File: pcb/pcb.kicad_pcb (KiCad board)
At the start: 2 copper layers, 126 x 50.5 mm, 53 parts, among them J1 Conn_01x02_Socket, J2 Conn_01x04_Socket, U1 AP2112K-3.3TRG1, U2 W25Q16JVUXIQ, U3 RP2040, U4 DS4432U+T&amp;R, U5 AD8403ARUZ1-REEL, U6 ADG801BRTZ-REEL7, Y2 Crystal_GND24_Small

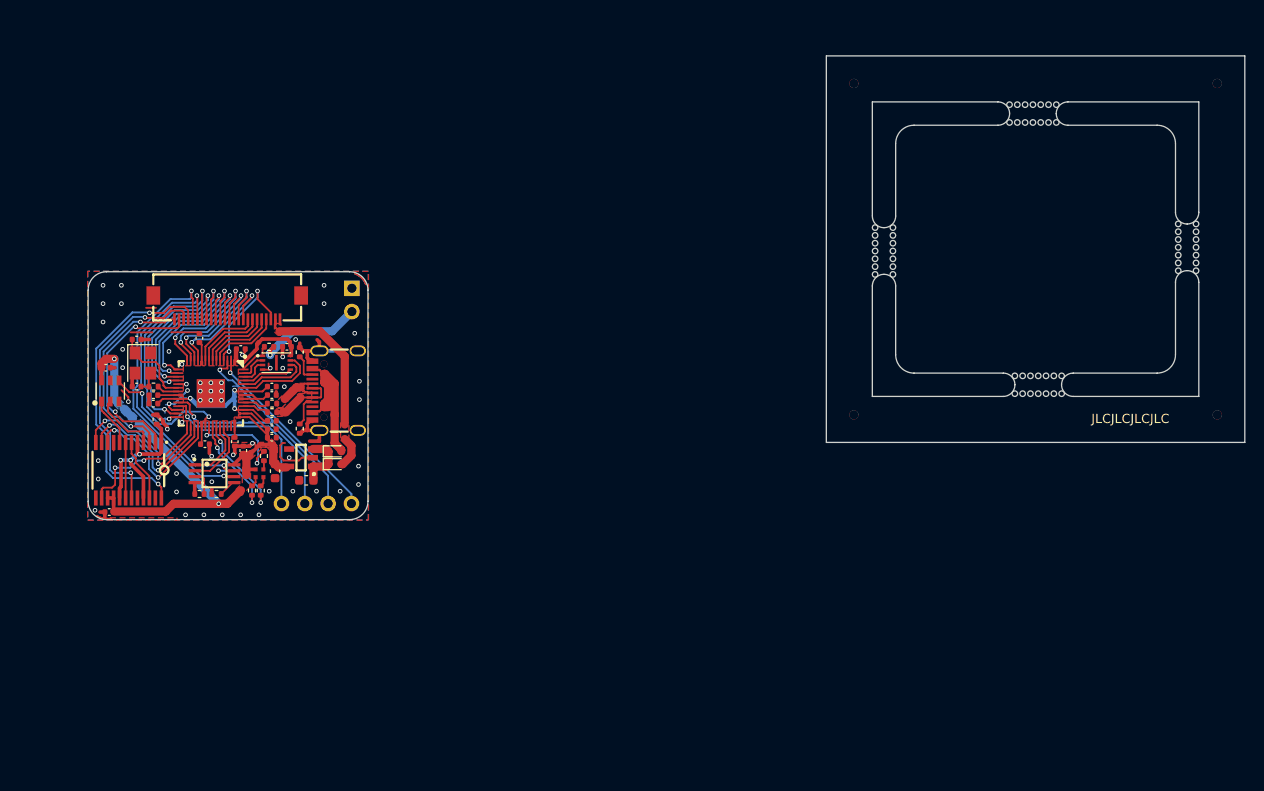
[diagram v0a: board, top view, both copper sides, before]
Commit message: Tweak holes
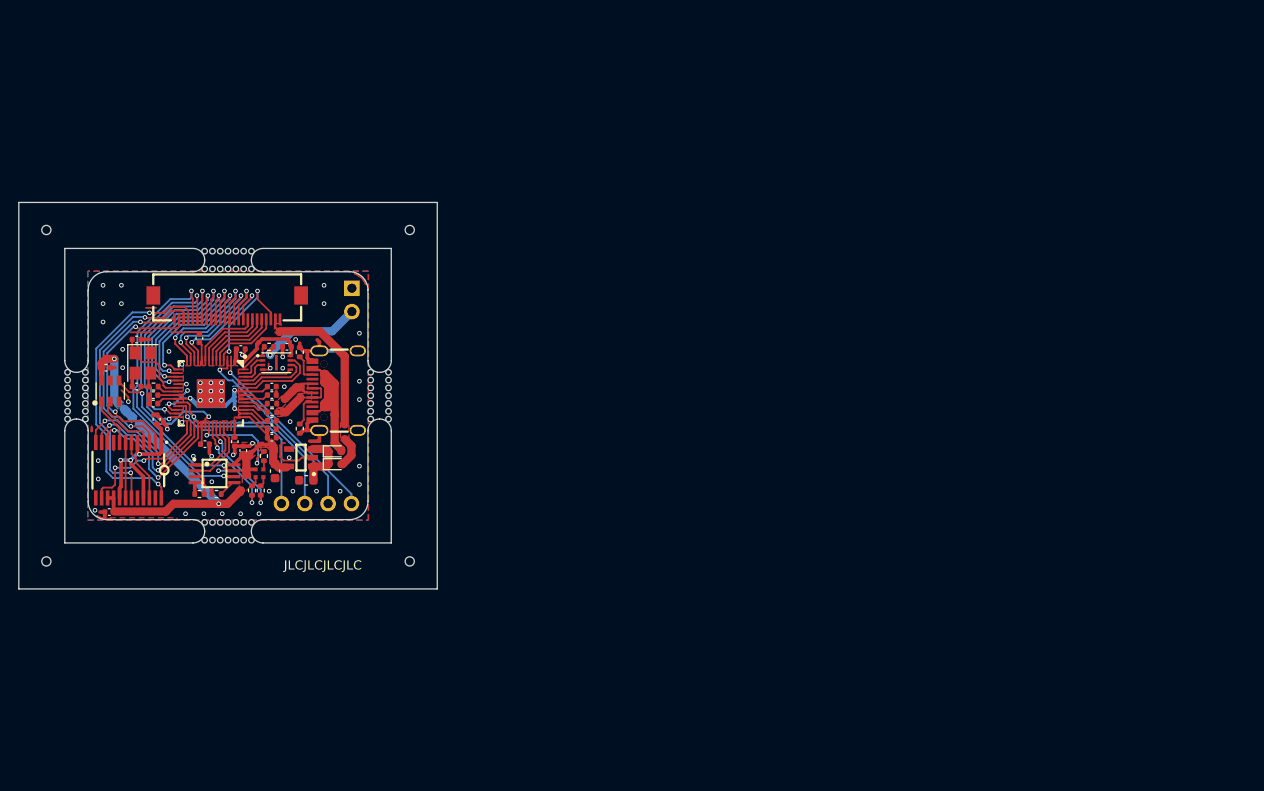
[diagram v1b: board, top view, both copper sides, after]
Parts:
- removed the REF** at (229.6, 29.5)
- removed the REF** at (190.0, 65.6)
- removed the REF** at (190.0, 29.5)
- removed the REF** at (229.6, 65.6)
- added REF**: Hole_1, MouseBites_2.54:Hole_1, F.Cu at (141.6, 81.5)
- added REF**: Hole_1, MouseBites_2.54:Hole_1, F.Cu at (102.0, 81.5)
- added REF**: Hole_1, MouseBites_2.54:Hole_1, F.Cu at (141.6, 45.5)
- added REF**: Hole_1, MouseBites_2.54:Hole_1, F.Cu at (102.0, 45.5)
- moved REF** 89.7 mm to (121.8, 79.5)
- moved REF** 89.4 mm to (139.6, 63.5)
- moved REF** 89.4 mm to (104.1, 63.5)
- moved REF** 89.1 mm to (121.8, 47.5)
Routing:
- net GND: track 53.9 -> 54.9 mm
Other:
- board size 126 x 50.5 mm -> 45.6 x 42.1 mm
- board text added: "Error:5 Warning:5"

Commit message: Resize
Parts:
- moved REF** 20.0 mm to (141.6, 25.4)
- moved REF** 20.0 mm to (102.0, 25.4)
- moved REF** 20.0 mm to (141.6, 101.5)
- moved REF** 20.0 mm to (102.0, 101.5)
- moved C11 1.43 mm to (123.8, 67.8), turned to 0 degrees
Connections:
- net RELAY_A renamed SW_IN
- LED1 pad 1: +3V3 -> LED_ANODE
- R10 pad 1: Net-(U3-GPIO23) -> LED_RED
- R11 pad 2: Net-(U3-GPIO24) -> LED_GREEN
- R12 pad 2: Net-(U3-GPIO25) -> LED_BLUE
- U3 pad 35: Net-(U3-GPIO23) -> LED_ANODE
- U3 pad 36: Net-(U3-GPIO24) -> LED_RED
- U3 pad 37: Net-(U3-GPIO25) -> LED_GREEN
- U3 pad 40: unconnected-(U3-GPIO28_ADC2-Pad40) -> LED_BLUE
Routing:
- net LED_GREEN: track 0.00 -> 13.2 mm, vias 0 -> 2
- net LED_BLUE: track 0.00 -> 12.2 mm, vias 0 -> 2
- net Net-(U3-GPIO25): track 11.2 -> 0.00 mm, vias 2 -> 0
- net Net-(U3-GPIO23): track 11.0 -> 0.00 mm, vias 2 -> 0
- net Net-(U3-GPIO24): track 10.9 -> 0.00 mm, vias 2 -> 0
- net LED_ANODE: track 0.00 -> 9.84 mm, vias 0 -> 2
- net LED_RED: track 0.00 -> 8.16 mm, vias 0 -> 2
- net +3V3: track 87.4 -> 86.7 mm
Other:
- board size 45.6 x 42.1 mm -> 45.6 x 82.1 mm

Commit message: Update PCB
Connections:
- U3 pad 35: LED_ANODE -> LED_RED
- U3 pad 36: LED_RED -> LED_GREEN
- U3 pad 37: LED_GREEN -> LED_ANODE
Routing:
- net LED_GREEN: track 13.2 -> 11.8 mm
- net LED_ANODE: track 9.84 -> 11.2 mm
- net LED_BLUE: track 12.2 -> 11.5 mm
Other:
- board text added: "https://github.com/ U-1F992/qingpi"
- board text removed: "NeoCtrlMod"
- board text removed: "https://github.com/ U-1F992/NeoCtrlMod"
